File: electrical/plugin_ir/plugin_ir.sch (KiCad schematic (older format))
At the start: 2 parts, among them Q2 AO3400

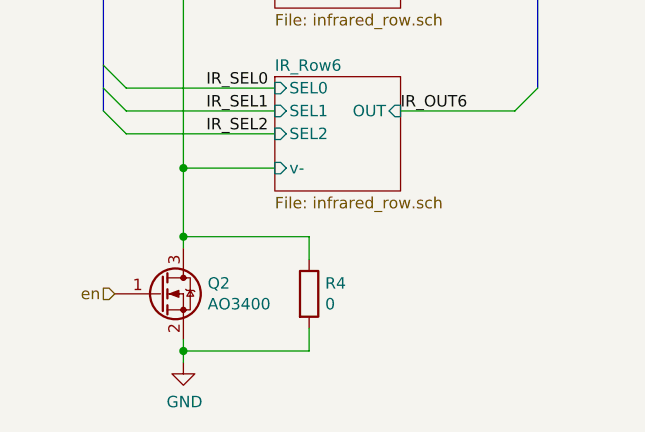
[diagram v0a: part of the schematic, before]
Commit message: Project divided into Core and Plugins
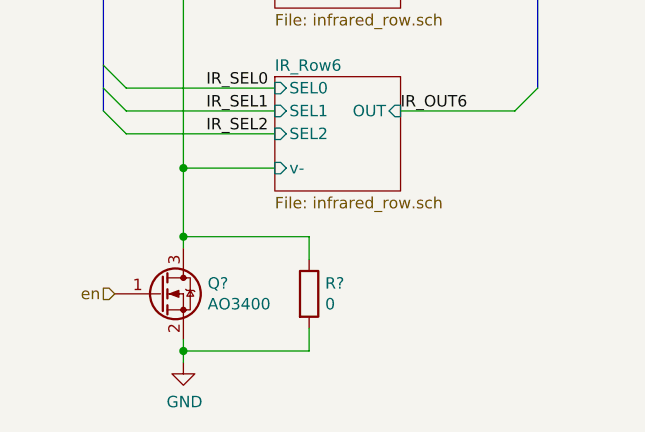
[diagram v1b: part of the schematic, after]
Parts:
- renumbered Q2 to Q?, R4 to R?
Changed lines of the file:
@@
 $Descr A4 11693 8268
 encoding utf-8
-Sheet 4 13
+Sheet 1 8
 Title ""
 Date ""
@@
 IR_OUT6
 $Comp
-L power:GND #PWR031
+L power:GND #PWR?
 U 1 1 5D41F6C3
 P 5300 7250
-F 0 "#PWR031" H 5300 7000 50  0001 C CNN
+F 0 "#PWR?" H 5300 7000 50  0001 C CNN
 F 1 "GND" H 5305 7077 50  0000 C CNN
 F 2 "" H 5300 7250 50  0001 C CNN
@@
 	5300 6750 5300 6700
 $Comp
-L Device:R R4
+L Device:R R?
 U 1 1 5D3ABC64
 P 5850 6950
-F 0 "R4" H 5920 6996 50  0000 L CNN
+F 0 "R?" H 5920 6996 50  0000 L CNN
 F 1 "0" H 5920 6905 50  0000 L CNN
 F 2 "Resistor_SMD:R_0805_2012Metric" V 5780 6950 50  0001 C CNN
@@
 	4950 1000 4950 6150
 $Comp
-L rasbot:AO3400 Q2
+L rasbot:AO3400 Q?
 U 1 1 5D3E0C2F
 P 5150 6950
-F 0 "Q2" H 5406 6996 50  0000 L CNN
+F 0 "Q?" H 5406 6996 50  0000 L CNN
 F 1 "AO3400" H 5406 6905 50  0000 L CNN
 F 2 "Package_TO_SOT_SMD:SOT-23" H 5975 6875 50  0001 C CNN
